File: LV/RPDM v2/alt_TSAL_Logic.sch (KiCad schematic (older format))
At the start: 9 parts

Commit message: rpdm
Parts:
- removed R?: 180k, symbol Device:R
- removed R?: 10, symbol Device:R
- removed R?: 10k, symbol Device:R
- added R?: 100k, symbol Device:R
- added R? (x2): 10k, symbol Device:R
- added RV?: 100k, symbol Device2:R_Potentiometer_Trim
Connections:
- net labels added: TSAT
- net labels removed: TSAT_Trigger
- wire segments 22 -> 27
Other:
- note added: "Green TSAL turns off with TSAT"
- note added: "Square wave flash circuit for red TSAL\nFrequency appox. 3Hz"
- note removed: "Frequency appox. 3Hz"
- moved on the sheet: C?, R2606, R?, U?

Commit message: rpdm
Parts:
- removed Q?: Q_NMOS_DGS, symbol Device2:Q_NMOS_DGS
- removed Q?: Q_PMOS_SGD, symbol Device2:Q_PMOS_SGD
- removed R? (x2): 10k, symbol Device:R
- removed U?: 74AHC1G14, symbol 74xGxx:74AHC1G14
- added Q3: Q_Dual_PMOS, symbol Device2:Q_Dual_PMOS_G1S2G2D2S1D1
- added R29, R32: 100k, symbol Device:R
- added R? (x2): 470, symbol Device:R
- added U4: 74LVC1G14, symbol 74xGxx:74LVC1G14
- added U5: 74AHC1G00, symbol 74xGxx:74AHC1G00
- gave numbers to parts that had none: 4
- renumbered R2606 to R31
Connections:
- net labels added: NAND_Out
- wire segments 27 -> 38
- no-connect marks 0 -> 1
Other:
- note added: "Green TSAL"
- note added: "NAND ensures red TSAL only\nflashes when TSAT is HIGH"
- note added: "Red TSAL"
- note added: "Square wave generator - 2-5.5 Hz\nSchmitt trigger configured as an astable multivibrator"
- note added: "Turns off with TSAT"
- note added: "Turns on with TSAT,\nflashes with square wave generator"
- note removed: "Green TSAL turns off with TSAT"
- note removed: "Square wave flash circuit for red TSAL\nFrequency appox. 3Hz"
- moved on the sheet: C8, R30, R31, R33, RV2

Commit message: rPDM - Started on board layout
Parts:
- C6: renamed from C8; footprint (none) -> Capacitor_SMD:C_0805_2012Metric_Pad1.15x1.40mm_HandSolder
- R3: renamed from R30; footprint (none) -> Resistor_SMD:R_0805_2012Metric_Pad1.15x1.40mm_HandSolder
- R4: renamed from R29; footprint (none) -> Resistor_SMD:R_0805_2012Metric_Pad1.15x1.40mm_HandSolder
- R5: renamed from R32; footprint (none) -> Resistor_SMD:R_0805_2012Metric_Pad1.15x1.40mm_HandSolder
- R6, R7: renamed from R?; footprint (none) -> Resistor_SMD:R_0805_2012Metric_Pad1.15x1.40mm_HandSolder
- R8: renamed from R31; footprint (none) -> Resistor_SMD:R_0805_2012Metric_Pad1.15x1.40mm_HandSolder
- R9: renamed from R33; footprint (none) -> Resistor_SMD:R_0805_2012Metric_Pad1.15x1.40mm_HandSolder
- renumbered Q3 to Q1, U4 to U3, U5 to U4
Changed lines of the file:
@@
 $Descr A4 11693 8268
 encoding utf-8
-Sheet 32 32
+Sheet 5 32
 Title "TSAL Circuit"
 Date "2021-06-28"
@@
 P 8750 3500
 AR Path="/5E553DA0/5E7ED9B4" Ref="R?"  Part="1"
-AR Path="/6106042D/5E7ED9B4" Ref="R31"  Part="1"
-F 0 "R31" V 8650 3500 50  0000 C CNN
+AR Path="/6106042D/5E7ED9B4" Ref="R8"  Part="1"
+F 0 "R8" V 8650 3500 50  0000 C CNN
 F 1 "10k" V 8850 3500 50  0000 C CNN
-F 2 "" V 8680 3500 50  0001 C CNN
+F 2 "Resistor_SMD:R_0805_2012Metric_Pad1.15x1.40mm_HandSolder" V 8680 3500 50  0001 C CNN
 F 3 "~" H 8750 3500 50  0001 C CNN
 	1    8750 3500
@@
 P 3500 2500
 AR Path="/5E553DA0/611F4C24" Ref="R?"  Part="1"
-AR Path="/6106042D/611F4C24" Ref="R30"  Part="1"
-F 0 "R30" V 3300 2500 50  0000 C CNN
+AR Path="/6106042D/611F4C24" Ref="R3"  Part="1"
+F 0 "R3" V 3300 2500 50  0000 C CNN
 F 1 "100k" V 3400 2500 50  0000 C CNN
-F 2 "" V 3430 2500 50  0001 C CNN
+F 2 "Resistor_SMD:R_0805_2012Metric_Pad1.15x1.40mm_HandSolder" V 3430 2500 50  0001 C CNN
 F 3 "~" H 3500 2500 50  0001 C CNN
 	1    3500 2500
@@
 P 8750 5500
 AR Path="/5E553DA0/6108A962" Ref="R?"  Part="1"
-AR Path="/6106042D/6108A962" Ref="R33"  Part="1"
-F 0 "R33" V 8650 5500 50  0000 C CNN
+AR Path="/6106042D/6108A962" Ref="R9"  Part="1"
+F 0 "R9" V 8650 5500 50  0000 C CNN
 F 1 "10k" V 8850 5500 50  0000 C CNN
-F 2 "" V 8680 5500 50  0001 C CNN
+F 2 "Resistor_SMD:R_0805_2012Metric_Pad1.15x1.40mm_HandSolder" V 8680 5500 50  0001 C CNN
 F 3 "~" H 8750 5500 50  0001 C CNN
 	1    8750 5500
@@
 P 3000 3500
 AR Path="/5E553DA0/5E7D702C" Ref="#PWR?"  Part="1"
-AR Path="/6106042D/5E7D702C" Ref="#PWR039"  Part="1"
-F 0 "#PWR039" H 3000 3250 50  0001 C CNN
+AR Path="/6106042D/5E7D702C" Ref="#PWR08"  Part="1"
+F 0 "#PWR08" H 3000 3250 50  0001 C CNN
 F 1 "GND" H 3000 3350 50  0000 C CNN
 F 2 "" H 3000 3500 50  0001 C CNN
@@
 P 3000 3250
 AR Path="/5E553DA0/61066862" Ref="C?"  Part="1"
-AR Path="/6106042D/61066862" Ref="C8"  Part="1"
-F 0 "C8" H 3115 3296 50  0000 L CNN
+AR Path="/6106042D/61066862" Ref="C6"  Part="1"
+F 0 "C6" H 3115 3296 50  0000 L CNN
 F 1 "1uF" H 3115 3205 50  0000 L CNN
-F 2 "" H 3038 3100 50  0001 C CNN
+F 2 "Capacitor_SMD:C_0805_2012Metric_Pad1.15x1.40mm_HandSolder" H 3038 3100 50  0001 C CNN
 F 3 "~" H 3000 3250 50  0001 C CNN
 	1    3000 3250
@@
 P 7500 5500
 AR Path="/5E553DA0/610682C2" Ref="#PWR?"  Part="1"
-AR Path="/6106042D/610682C2" Ref="#PWR043"  Part="1"
-F 0 "#PWR043" H 7500 5250 50  0001 C CNN
+AR Path="/6106042D/610682C2" Ref="#PWR012"  Part="1"
+F 0 "#PWR012" H 7500 5250 50  0001 C CNN
 F 1 "GND" H 7500 5350 50  0000 C CNN
 F 2 "" H 7500 5500 50  0001 C CNN
@@
 P 7500 5250
 AR Path="/5E553DA0/610682CE" Ref="R?"  Part="1"
-AR Path="/6106042D/610682CE" Ref="R32"  Part="1"
-F 0 "R32" H 7450 5250 50  0000 R TNN
+AR Path="/6106042D/610682CE" Ref="R5"  Part="1"
+F 0 "R5" H 7450 5250 50  0000 R TNN
 F 1 "100k" H 7450 5325 50  0000 R TNN
-F 2 "" V 7430 5250 50  0001 C CNN
+F 2 "Resistor_SMD:R_0805_2012Metric_Pad1.15x1.40mm_HandSolder" V 7430 5250 50  0001 C CNN
 F 3 "~" H 7500 5250 50  0001 C CNN
 	1    7500 5250
@@
 	8500 2500 8500 2800
 $Comp
-L 74xGxx:74AHC1G00 U5
+L 74xGxx:74AHC1G00 U4
 U 1 1 61074F10
 P 5000 3000
-F 0 "U5" H 5100 3050 50  0000 L BNN
+F 0 "U4" H 5100 3050 50  0000 L BNN
 F 1 "74AHC1G00" H 5100 2950 50  0000 L TNN
 F 2 "" H 5000 3000 50  0001 C CNN
@@
 $EndComp
 $Comp
-L 74xGxx:74LVC1G14 U4
+L 74xGxx:74LVC1G14 U3
 U 1 1 610761FD
 P 3500 3000
-F 0 "U4" H 3550 3050 50  0000 L BNN
+F 0 "U3" H 3550 3050 50  0000 L BNN
 F 1 "74LVC1G14" H 3550 2950 50  0000 L TNN
 F 2 "" H 3500 3000 50  0001 C CNN
@@
 P 3500 3500
 AR Path="/5E553DA0/6107A77A" Ref="#PWR?"  Part="1"
-AR Path="/6106042D/6107A77A" Ref="#PWR041"  Part="1"
-F 0 "#PWR041" H 3500 3250 50  0001 C CNN
+AR Path="/6106042D/6107A77A" Ref="#PWR09"  Part="1"
+F 0 "#PWR09" H 3500 3250 50  0001 C CNN
 F 1 "GND" H 3500 3350 50  0000 C CNN
 F 2 "" H 3500 3500 50  0001 C CNN
@@
 P 5000 3500
 AR Path="/5E553DA0/61096492" Ref="#PWR?"  Part="1"
-AR Path="/6106042D/61096492" Ref="#PWR042"  Part="1"
-F 0 "#PWR042" H 5000 3250 50  0001 C CNN
+AR Path="/6106042D/61096492" Ref="#PWR010"  Part="1"
+F 0 "#PWR010" H 5000 3250 50  0001 C CNN
 F 1 "GND" H 5000 3350 50  0000 C CNN
 F 2 "" H 5000 3500 50  0001 C CNN
@@
 P 7500 3500
 AR Path="/5E553DA0/610BFA92" Ref="#PWR?"  Part="1"
-AR Path="/6106042D/610BFA92" Ref="#PWR040"  Part="1"
-F 0 "#PWR040" H 7500 3250 50  0001 C CNN
+AR Path="/6106042D/610BFA92" Ref="#PWR011"  Part="1"
+F 0 "#PWR011" H 7500 3250 50  0001 C CNN
 F 1 "GND" H 7500 3350 50  0000 C CNN
 F 2 "" H 7500 3500 50  0001 C CNN
@@
 P 7500 3250
 AR Path="/5E553DA0/610BFA9E" Ref="R?"  Part="1"
-AR Path="/6106042D/610BFA9E" Ref="R29"  Part="1"
-F 0 "R29" H 7450 3250 50  0000 R TNN
+AR Path="/6106042D/610BFA9E" Ref="R4"  Part="1"
+F 0 "R4" H 7450 3250 50  0000 R TNN
 F 1 "100k" H 7450 3325 50  0000 R TNN
-F 2 "" V 7430 3250 50  0001 C CNN
+F 2 "Resistor_SMD:R_0805_2012Metric_Pad1.15x1.40mm_HandSolder" V 7430 3250 50  0001 C CNN
 F 3 "~" H 7500 3250 50  0001 C CNN
 	1    7500 3250
@@
 	6000 4000 10000 4000
 $Comp
-L Device2:Q_Dual_PMOS_G1S2G2D2S1D1 Q3
+L Device2:Q_Dual_PMOS_G1S2G2D2S1D1 Q1
 U 1 1 61140713
 P 8400 3000
-F 0 "Q3" H 8605 2954 50  0000 L CNN
+F 0 "Q1" H 8605 2954 50  0000 L CNN
 F 1 "Q_Dual_PMOS" H 8605 3045 50  0000 L CNN
 F 2 "" H 8450 3000 50  0001 C CNN
@@
 $EndComp
 $Comp
-L Device2:Q_Dual_PMOS_G1S2G2D2S1D1 Q3
+L Device2:Q_Dual_PMOS_G1S2G2D2S1D1 Q1
 U 2 1 61142490
 P 8400 5000
-F 0 "Q3" H 8605 4954 50  0000 L CNN
+F 0 "Q1" H 8605 4954 50  0000 L CNN
 F 1 "Q_Dual_PMOS" H 8605 5045 50  0000 L CNN
 F 2 "" H 8450 5000 50  0001 C CNN
@@
 P 8000 3000
 AR Path="/5E553DA0/617FB17B" Ref="R?"  Part="1"
-AR Path="/6106042D/617FB17B" Ref="R?"  Part="1"
-F 0 "R?" V 7900 3000 50  0000 C CNN
+AR Path="/6106042D/617FB17B" Ref="R6"  Part="1"
+F 0 "R6" V 7900 3000 50  0000 C CNN
 F 1 "470" V 8100 3000 50  0000 C CNN
-F 2 "" V 7930 3000 50  0001 C CNN
+F 2 "Resistor_SMD:R_0805_2012Metric_Pad1.15x1.40mm_HandSolder" V 7930 3000 50  0001 C CNN
 F 3 "~" H 8000 3000 50  0001 C CNN
 	1    8000 3000
@@
 P 8000 5000
 AR Path="/5E553DA0/61800B35" Ref="R?"  Part="1"
-AR Path="/6106042D/61800B35" Ref="R?"  Part="1"
-F 0 "R?" V 7900 5000 50  0000 C CNN
+AR Path="/6106042D/61800B35" Ref="R7"  Part="1"
+F 0 "R7" V 7900 5000 50  0000 C CNN
 F 1 "470" V 8100 5000 50  0000 C CNN
-F 2 "" V 7930 5000 50  0001 C CNN
+F 2 "Resistor_SMD:R_0805_2012Metric_Pad1.15x1.40mm_HandSolder" V 7930 5000 50  0001 C CNN
 F 3 "~" H 8000 5000 50  0001 C CNN
 	1    8000 5000

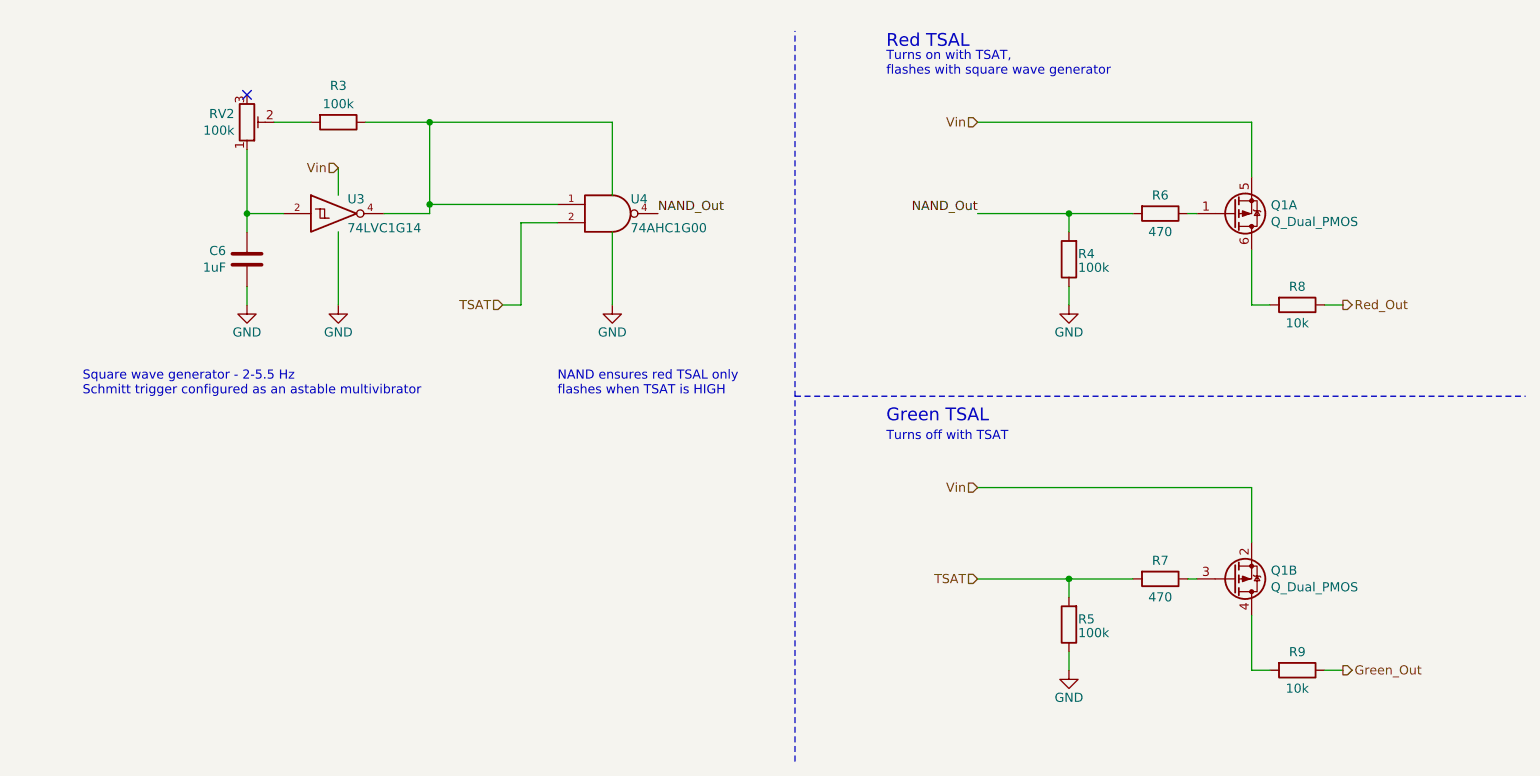
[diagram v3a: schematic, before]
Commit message: rpdm, libraries cleanup
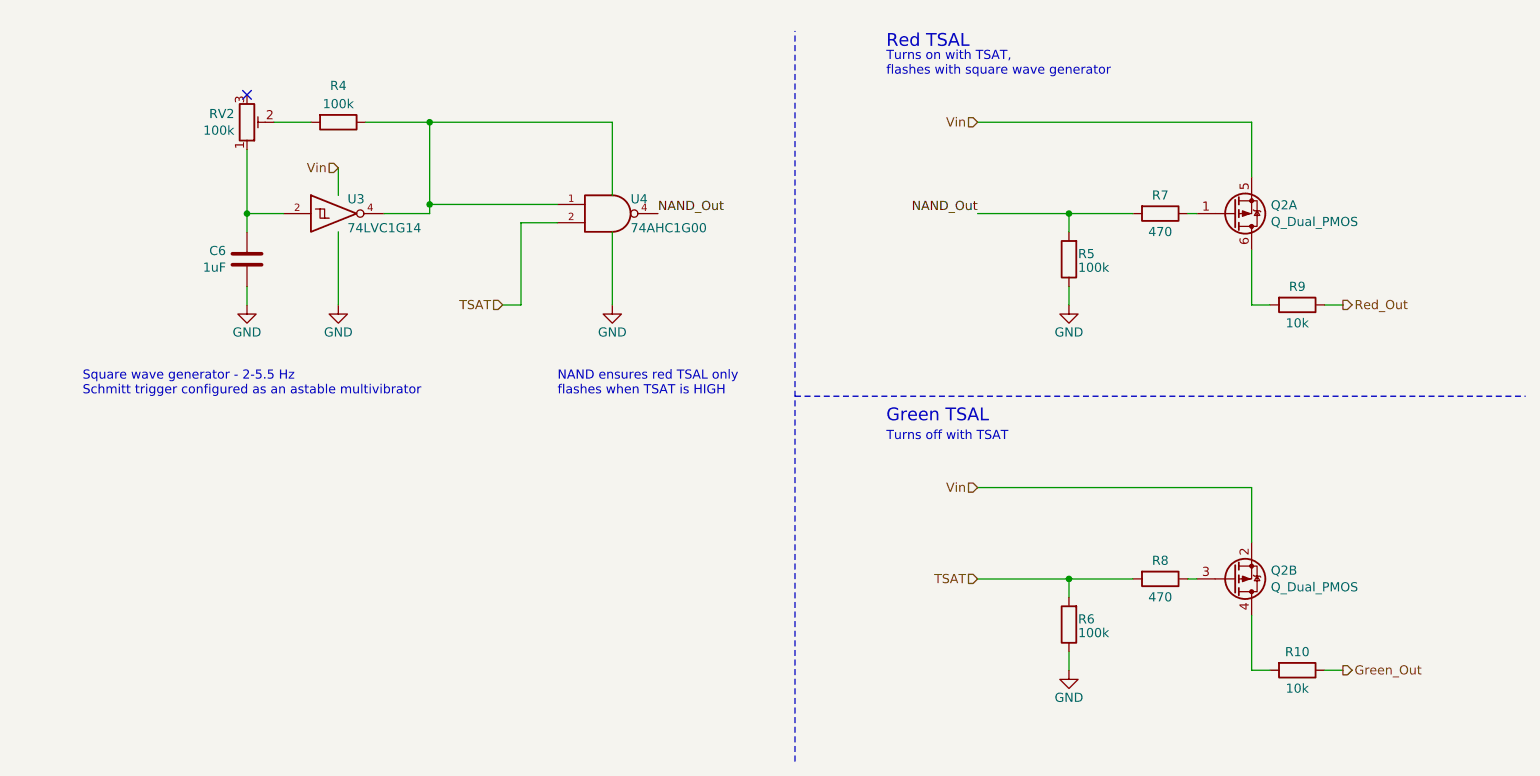
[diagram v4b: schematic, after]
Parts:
- renumbered Q1 to Q2, R9 to R10, R3 to R4, R4 to R5, R5 to R6, R6 to R7, R7 to R8, R8 to R9
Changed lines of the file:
@@
 P 8750 3500
 AR Path="/5E553DA0/5E7ED9B4" Ref="R?"  Part="1"
-AR Path="/6106042D/5E7ED9B4" Ref="R8"  Part="1"
-F 0 "R8" V 8650 3500 50  0000 C CNN
+AR Path="/6106042D/5E7ED9B4" Ref="R9"  Part="1"
+F 0 "R9" V 8650 3500 50  0000 C CNN
 F 1 "10k" V 8850 3500 50  0000 C CNN
 F 2 "Resistor_SMD:R_0805_2012Metric_Pad1.15x1.40mm_HandSolder" V 8680 3500 50  0001 C CNN
@@
 P 3500 2500
 AR Path="/5E553DA0/611F4C24" Ref="R?"  Part="1"
-AR Path="/6106042D/611F4C24" Ref="R3"  Part="1"
-F 0 "R3" V 3300 2500 50  0000 C CNN
+AR Path="/6106042D/611F4C24" Ref="R4"  Part="1"
+F 0 "R4" V 3300 2500 50  0000 C CNN
 F 1 "100k" V 3400 2500 50  0000 C CNN
 F 2 "Resistor_SMD:R_0805_2012Metric_Pad1.15x1.40mm_HandSolder" V 3430 2500 50  0001 C CNN
@@
 P 8750 5500
 AR Path="/5E553DA0/6108A962" Ref="R?"  Part="1"
-AR Path="/6106042D/6108A962" Ref="R9"  Part="1"
-F 0 "R9" V 8650 5500 50  0000 C CNN
+AR Path="/6106042D/6108A962" Ref="R10"  Part="1"
+F 0 "R10" V 8650 5500 50  0000 C CNN
 F 1 "10k" V 8850 5500 50  0000 C CNN
 F 2 "Resistor_SMD:R_0805_2012Metric_Pad1.15x1.40mm_HandSolder" V 8680 5500 50  0001 C CNN
@@
 P 7500 5250
 AR Path="/5E553DA0/610682CE" Ref="R?"  Part="1"
-AR Path="/6106042D/610682CE" Ref="R5"  Part="1"
-F 0 "R5" H 7450 5250 50  0000 R TNN
+AR Path="/6106042D/610682CE" Ref="R6"  Part="1"
+F 0 "R6" H 7450 5250 50  0000 R TNN
 F 1 "100k" H 7450 5325 50  0000 R TNN
 F 2 "Resistor_SMD:R_0805_2012Metric_Pad1.15x1.40mm_HandSolder" V 7430 5250 50  0001 C CNN
@@
 P 7500 3250
 AR Path="/5E553DA0/610BFA9E" Ref="R?"  Part="1"
-AR Path="/6106042D/610BFA9E" Ref="R4"  Part="1"
-F 0 "R4" H 7450 3250 50  0000 R TNN
+AR Path="/6106042D/610BFA9E" Ref="R5"  Part="1"
+F 0 "R5" H 7450 3250 50  0000 R TNN
 F 1 "100k" H 7450 3325 50  0000 R TNN
 F 2 "Resistor_SMD:R_0805_2012Metric_Pad1.15x1.40mm_HandSolder" V 7430 3250 50  0001 C CNN
@@
 	6000 4000 10000 4000
 $Comp
-L Device2:Q_Dual_PMOS_G1S2G2D2S1D1 Q1
+L Device2:Q_Dual_PMOS_G1S2G2D2S1D1 Q2
 U 1 1 61140713
 P 8400 3000
-F 0 "Q1" H 8605 2954 50  0000 L CNN
+F 0 "Q2" H 8605 2954 50  0000 L CNN
 F 1 "Q_Dual_PMOS" H 8605 3045 50  0000 L CNN
 F 2 "" H 8450 3000 50  0001 C CNN
@@
 $EndComp
 $Comp
-L Device2:Q_Dual_PMOS_G1S2G2D2S1D1 Q1
+L Device2:Q_Dual_PMOS_G1S2G2D2S1D1 Q2
 U 2 1 61142490
 P 8400 5000
-F 0 "Q1" H 8605 4954 50  0000 L CNN
+F 0 "Q2" H 8605 4954 50  0000 L CNN
 F 1 "Q_Dual_PMOS" H 8605 5045 50  0000 L CNN
 F 2 "" H 8450 5000 50  0001 C CNN
@@
 P 8000 3000
 AR Path="/5E553DA0/617FB17B" Ref="R?"  Part="1"
-AR Path="/6106042D/617FB17B" Ref="R6"  Part="1"
-F 0 "R6" V 7900 3000 50  0000 C CNN
+AR Path="/6106042D/617FB17B" Ref="R7"  Part="1"
+F 0 "R7" V 7900 3000 50  0000 C CNN
 F 1 "470" V 8100 3000 50  0000 C CNN
 F 2 "Resistor_SMD:R_0805_2012Metric_Pad1.15x1.40mm_HandSolder" V 7930 3000 50  0001 C CNN
@@
 P 8000 5000
 AR Path="/5E553DA0/61800B35" Ref="R?"  Part="1"
-AR Path="/6106042D/61800B35" Ref="R7"  Part="1"
-F 0 "R7" V 7900 5000 50  0000 C CNN
+AR Path="/6106042D/61800B35" Ref="R8"  Part="1"
+F 0 "R8" V 7900 5000 50  0000 C CNN
 F 1 "470" V 8100 5000 50  0000 C CNN
 F 2 "Resistor_SMD:R_0805_2012Metric_Pad1.15x1.40mm_HandSolder" V 7930 5000 50  0001 C CNN

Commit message: RPDM
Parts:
- added C1, C3: 0.1µF, Capacitor_SMD:C_0603_1608Metric_Pad1.05x0.95mm_HandSolder, symbol Device:C
- Q1: renamed from Q2; footprint (none) -> Package_SO:TSOP-6_1.65x3.05mm_P0.95mm
- RV1: renamed from RV2; footprint (none) -> UOWM_Potentiometers:TRIM_3214W
- U1: renamed from U3; value 74LVC1G14 -> BU4S584G2; footprint (none) -> UOWM_Package_SO:SSOP-5_ROHM
- U2: renamed from U4; value 74AHC1G00 -> BU4S11G2; footprint (none) -> UOWM_Package_SO:SSOP-5_ROHM
- renumbered C6 to C2, R4 to R1, R5 to R2, R6 to R3, R7 to R4, R8 to R5, R9 to R6, R10 to R7
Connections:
- net GND: now also C1.2, C3.2; no longer R2.1
- net NAND_Out: now also R2.1; no longer R2.2
- net TSAT: now also U2.1; no longer U2.2
- net VCC: now also R2.2, C1.1, C3.1; no longer R1.1, U1.4, U2.1
- new net: R1.1, U1.4, U2.2
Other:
- note added: "NAND\nBypass"
- note added: "Schmitt\nBypass"
- moved on the sheet: R1, R2, RV1

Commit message: RPDM nearly finished
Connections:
- net at R6.2: now also Q1.4 (D); no longer Q1.6 (D)
- net at R7.2: now also Q1.6 (D); no longer Q1.4 (D)
- net at Q1.1 (G): now also R5.1; no longer R4.1
- net at Q1.3 (G): now also R4.1; no longer R5.1
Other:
- moved on the sheet: Q1A, Q1B
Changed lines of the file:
@@
 L Device2:Q_Dual_PMOS_G1S2G2D2S1D1 Q1
 U 1 1 61140713
+P 8400 5000
+F 0 "Q1" H 8605 4954 50  0000 L CNN
+F 1 "Q_Dual_PMOS" H 8605 5045 50  0000 L CNN
+F 2 "Package_SO:TSOP-6_1.65x3.05mm_P0.95mm" H 8450 5000 50  0001 C CNN
+F 3 "https://www.vishay.com/docs/75059/sq3989ev.pdf" H 8450 5000 50  0001 C CNN
+	1    8400 5000
+	1    0    0    1
+$EndComp
+$Comp
+L Device2:Q_Dual_PMOS_G1S2G2D2S1D1 Q1
+U 2 1 61142490
 P 8400 3000
 F 0 "Q1" H 8605 2954 50  0000 L CNN
@@
 F 2 "Package_SO:TSOP-6_1.65x3.05mm_P0.95mm" H 8450 3000 50  0001 C CNN
 F 3 "https://www.vishay.com/docs/75059/sq3989ev.pdf" H 8450 3000 50  0001 C CNN
-	1    8400 3000
+	2    8400 3000
 	1    0    0    1
 $EndComp
-$Comp
-L Device2:Q_Dual_PMOS_G1S2G2D2S1D1 Q1
-U 2 1 61142490
-P 8400 5000
-F 0 "Q1" H 8605 4954 50  0000 L CNN
-F 1 "Q_Dual_PMOS" H 8605 5045 50  0000 L CNN
-F 2 "Package_SO:TSOP-6_1.65x3.05mm_P0.95mm" H 8450 5000 50  0001 C CNN
-F 3 "https://www.vishay.com/docs/75059/sq3989ev.pdf" H 8450 5000 50  0001 C CNN
-	2    8400 5000
-	1    0    0    1
-$EndComp
